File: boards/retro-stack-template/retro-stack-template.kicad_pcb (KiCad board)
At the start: 2 copper layers, 99.1 x 99.1 mm, 7 parts, among them J1 BUS_6502

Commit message: Update template
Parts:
- added D1: LED_PWR, LED_THT:LED_D5.0mm, F.Cu at (113.0, 133.3)
- added J2: TRM_PWR, TerminalBlock_Phoenix:TerminalBlock_Phoenix_MPT-0,5-2-2.54_1x02_P2.54mm_Horizontal, F.Cu at (182.9, 41.9)
- added R1: 1k, Resistor_THT:R_Axial_DIN0204_L3.6mm_D1.6mm_P5.08mm_Horizontal, F.Cu at (113.0, 128.3)
- added kibuzzard-642C367F: G***, kibuzzard-642C367F, F.Cu at (118.7, 135.3)
- added kibuzzard-642C36EF: G***, kibuzzard-642C36EF, F.Cu at (174.6, 41.9)
- moved G*** 81.4 mm to (195.6, 127.0)
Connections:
- J1 pad 16: /VDD -> +5V
- J1 pad 39: /VSS -> GND
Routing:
- added copper zone on F.Cu, net +5V
- added copper zone on B.Cu, net GND
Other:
- board text added: "Board Template & External Power"
- board text added: "RetroStack"
- board text added: "©Microcode.io"

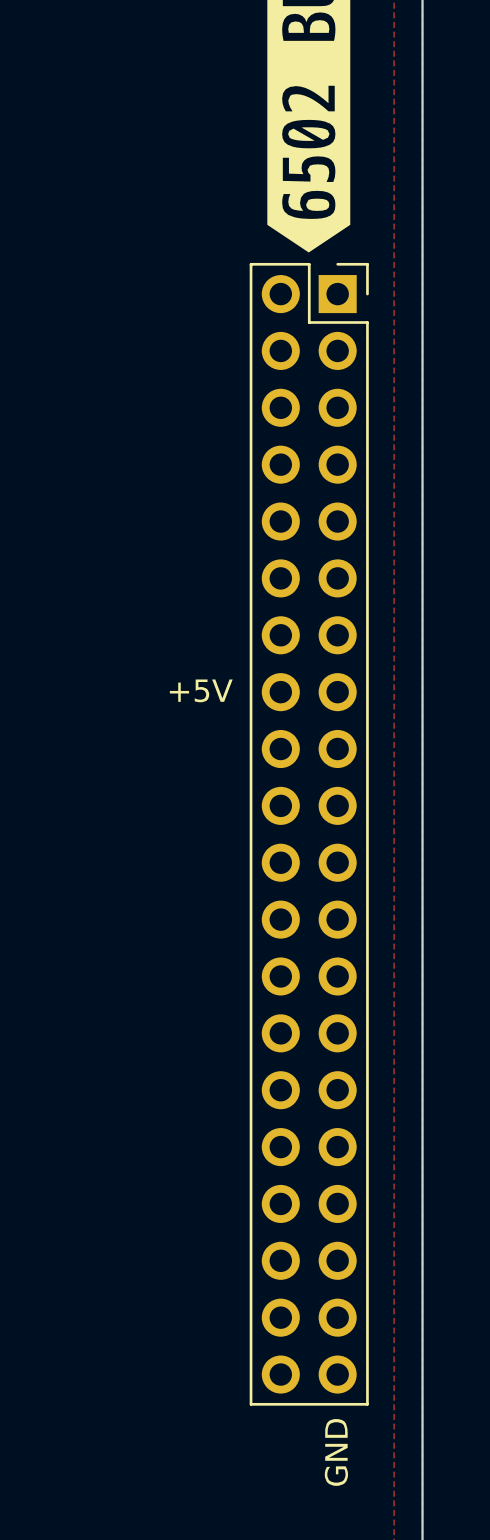
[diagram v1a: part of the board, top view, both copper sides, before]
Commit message: Update template to use right angle idc instead of vertical pin socket.
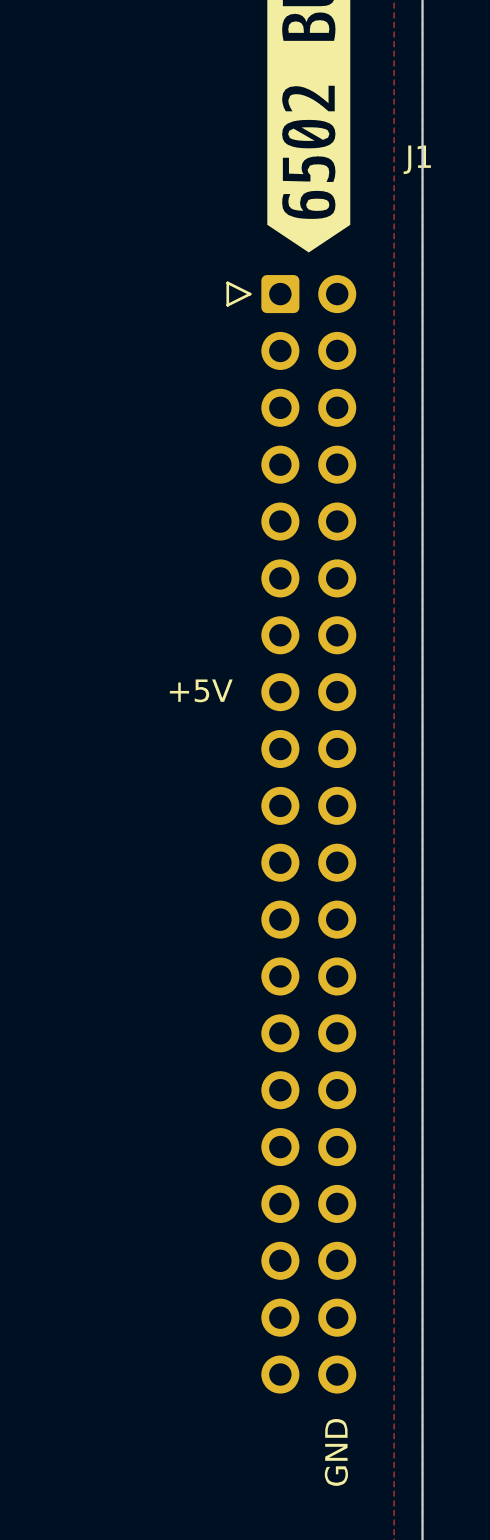
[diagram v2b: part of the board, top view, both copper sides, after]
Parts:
- J1: footprint Connector_PinSocket_2.54mm:PinSocket_2x20_P2.54mm_Vertical -> Connector_IDC:IDC-Header_2x20_P2.54mm_Horizontal
- moved J1 2.56 mm to (194.3, 63.5)
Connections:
- J1 pad 1: /~{RES} -> /VPB
- J1 pad 10: /~{ML} -> /BE
- J1 pad 11: /NC -> /~{NMI}
- J1 pad 12: /~{NMI} -> /NC
- J1 pad 13: /R/~{W} -> /SYNC
- J1 pad 14: /SYNC -> /R/~{W}
- J1 pad 15: /D0 -> +5V
- J1 pad 16: +5V -> /D0
- J1 pad 17: /D1 -> /A0
- J1 pad 18: /A0 -> /D1
- J1 pad 19: /D2 -> /A1
- J1 pad 2: /VPB -> /~{RES}
- J1 pad 20: /A1 -> /D2
- J1 pad 21: /D3 -> /A2
- J1 pad 22: /A2 -> /D3
- J1 pad 23: /D4 -> /A3
- J1 pad 24: /A3 -> /D4
- J1 pad 25: /D5 -> /A4
- J1 pad 26: /A4 -> /D5
- J1 pad 27: /D6 -> /A5
- J1 pad 28: /A5 -> /D6
- J1 pad 29: /D7 -> /A6
- J1 pad 3: /PHI2O -> /RDY
- J1 pad 30: /A6 -> /D7
- J1 pad 31: /A15 -> /A7
- J1 pad 32: /A7 -> /A15
- J1 pad 33: /A14 -> /A8
- J1 pad 34: /A8 -> /A14
- J1 pad 35: /A13 -> /A9
- J1 pad 36: /A9 -> /A13
- J1 pad 37: /A12 -> /A10
- J1 pad 38: /A10 -> /A12
- J1 pad 39: GND -> /A11
- J1 pad 4: /RDY -> /PHI2O
- J1 pad 40: /A11 -> GND
- J1 pad 5: /~{SO} -> /PHI1O
- J1 pad 6: /PHI1O -> /~{SO}
- J1 pad 7: /PHI2 -> /~{IRQ}
- J1 pad 8: /~{IRQ} -> /PHI2
- J1 pad 9: /BE -> /~{ML}
